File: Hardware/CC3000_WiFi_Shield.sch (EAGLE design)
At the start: 32 parts, among them J1 U.FL, U1 V_REG_317SMD, U2 ARDUINO_SHIELDLABEL, U3 74HC4050, U4 USD-SOCKETNEW, U5 CC3000

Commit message: Prototype board ready for review
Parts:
- C8: value 10pF -> DNP; COEFF C0G -> (none); PLACE DNP -> (none); TOL 5% -> (none)
- D1: value (none) -> GREEN; COLOR GREEN -> (none)
- JP1: value (none) -> Debug
- SJ1: value (none) -> Mode
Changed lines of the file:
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@@
 <setting verticaltext="up"/>
 </settings>
-<grid distance="0.1" unitdist="inch" unit="inch" style="lines" multiple="1" display="yes" altdistance="0.01" altunitdist="inch" altunit="inch"/>
+<grid distance="0.1" unitdist="inch" unit="inch" style="lines" multiple="1" display="no" altdistance="0.01" altunitdist="inch" altunit="inch"/>
 <layers>
 <layer number="1" name="Top" color="4" fill="1" visible="no" active="no"/>
@@
 <part name="SUPPLY5" library="SparkFun-Aesthetics" deviceset="3.3V" device=""/>
 <part name="GND9" library="SparkFun-Aesthetics" deviceset="GND" device=""/>
-<part name="SJ1" library="SparkFun-Passives" deviceset="SOLDERJUMPER_2WAY" device="PASTE1&amp;2"/>
+<part name="SJ1" library="SparkFun-Passives" deviceset="SOLDERJUMPER_2WAY" device="PASTE1&amp;2" value="Mode"/>
 <part name="GND10" library="SparkFun-Aesthetics" deviceset="GND" device=""/>
 <part name="GND11" library="SparkFun-Aesthetics" deviceset="GND" device=""/>
@@
 <part name="GND16" library="SparkFun-Aesthetics" deviceset="GND" device=""/>
 <part name="GND17" library="SparkFun-Aesthetics" deviceset="GND" device=""/>
-<part name="JP1" library="SparkFun-Connectors" deviceset="M03" device="PTH"/>
+<part name="JP1" library="SparkFun-Connectors" deviceset="M03" device="PTH" value="Debug"/>
 <part name="GND18" library="SparkFun-Aesthetics" deviceset="GND" device=""/>
-<part name="C8" library="SparkFun-Capacitors" deviceset="CAP" device="0603-CAP" value="10pF">
-<attribute name="COEFF" value="C0G"/>
-<attribute name="PLACE" value="DNP"/>
-<attribute name="TOL" value="5%"/>
-</part>
+<part name="C8" library="SparkFun-Capacitors" deviceset="CAP" device="0603-CAP" value="DNP"/>
 <part name="C7" library="SparkFun-Capacitors" deviceset="CAP" device="0603-CAP" value="2.2pF">
 <attribute name="COEFF" value="C0G"/>
@@
 <part name="R3" library="SparkFun-Resistors" deviceset="RESISTOR" device="0603-RES" value="390"/>
 <part name="GND19" library="SparkFun-Aesthetics" deviceset="GND" device=""/>
-<part name="D1" library="SparkFun-LED" deviceset="LED-GREEN" device="0603">
-<attribute name="COLOR" value="GREEN"/>
-</part>
+<part name="D1" library="SparkFun-LED" deviceset="LED-GREEN" device="0603" value="GREEN"/>
 <part name="R4" library="SparkFun-Resistors" deviceset="RESISTOR" device="0603-RES" value="10k"/>
 <part name="R5" library="SparkFun-Resistors" deviceset="RESISTOR" device="0603-RES" value="10k"/>
@@
 <instance part="GND16" gate="1" x="127" y="144.78"/>
 <instance part="GND17" gate="1" x="149.86" y="144.78"/>
-<instance part="JP1" gate="G$1" x="38.1" y="121.92" rot="MR180"/>
+<instance part="JP1" gate="G$1" x="38.1" y="121.92" smashed="yes" rot="MR180">
+<attribute name="VALUE" x="25.4" y="127" size="1.778" layer="96" rot="MR180"/>
+<attribute name="NAME" x="35.56" y="116.078" size="1.778" layer="95" rot="MR180"/>
+</instance>
 <instance part="GND18" gate="1" x="50.8" y="114.3"/>
 <instance part="C8" gate="G$1" x="182.88" y="167.64" smashed="yes" rot="R90">
-<attribute name="COEFF" x="182.88" y="160.02" size="1.778" layer="96"/>
-<attribute name="TOL" x="182.88" y="162.56" size="1.778" layer="96"/>
 <attribute name="NAME" x="177.8" y="170.307" size="1.778" layer="95"/>
 <attribute name="VALUE" x="182.88" y="165.227" size="1.778" layer="96"/>
-<attribute name="PLACE" x="182.88" y="170.18" size="1.778" layer="96"/>
 </instance>
 <instance part="C7" gate="G$1" x="139.7" y="167.64" smashed="yes" rot="R90">
@@
 <instance part="GND19" gate="1" x="83.82" y="142.24"/>
 <instance part="D1" gate="G$1" x="83.82" y="157.48" smashed="yes">
-<attribute name="COLOR" x="86.36" y="154.94" size="1.778" layer="96"/>
 <attribute name="NAME" x="86.36" y="157.48" size="1.778" layer="95"/>
-<attribute name="VALUE" x="89.535" y="152.908" size="1.778" layer="96" rot="R90"/>
+<attribute name="VALUE" x="86.106" y="154.305" size="1.778" layer="96"/>
 </instance>
 <instance part="R4" gate="G$1" x="53.34" y="33.02" smashed="yes" rot="R90">
@@
 <wire x1="60.96" y1="175.26" x2="60.96" y2="172.72" width="0.1524" layer="91"/>
 <junction x="50.8" y="175.26"/>
-<pinref part="C4" gate="G$1" pin="1"/>
+<junction x="60.96" y="175.26"/>
+<pinref part="R3" gate="G$1" pin="2"/>
 <wire x1="60.96" y1="175.26" x2="71.12" y2="175.26" width="0.1524" layer="91"/>
-<wire x1="71.12" y1="175.26" x2="71.12" y2="172.72" width="0.1524" layer="91"/>
-<junction x="60.96" y="175.26"/>
-<junction x="71.12" y="175.26"/>
-<wire x1="71.12" y1="172.72" x2="71.12" y2="170.18" width="0.1524" layer="91"/>
-<pinref part="R3" gate="G$1" pin="2"/>
 <wire x1="71.12" y1="175.26" x2="83.82" y2="175.26" width="0.1524" layer="91"/>
 <wire x1="83.82" y1="175.26" x2="83.82" y2="172.72" width="0.1524" layer="91"/>
@@
 <wire x1="83.82" y1="177.8" x2="83.82" y2="175.26" width="0.1524" layer="91"/>
 <junction x="83.82" y="175.26"/>
+<pinref part="C4" gate="G$1" pin="1"/>
+<wire x1="71.12" y1="172.72" x2="71.12" y2="175.26" width="0.1524" layer="91"/>
+<junction x="71.12" y="175.26"/>
 </segment>
 <segment>
@@
 </sheet>
 </sheets>
+<errors>
+</errors>
 </schematic>
 </drawing>

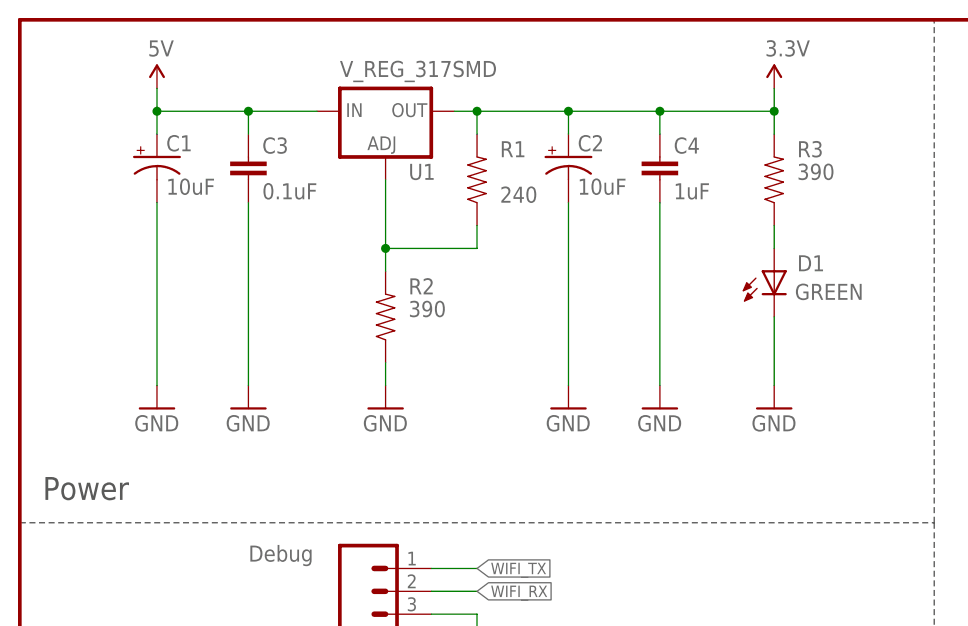
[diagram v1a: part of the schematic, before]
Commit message: Fixed floating 3.3V paddle on LM317. Made stitching vias near RF section 10 mils.
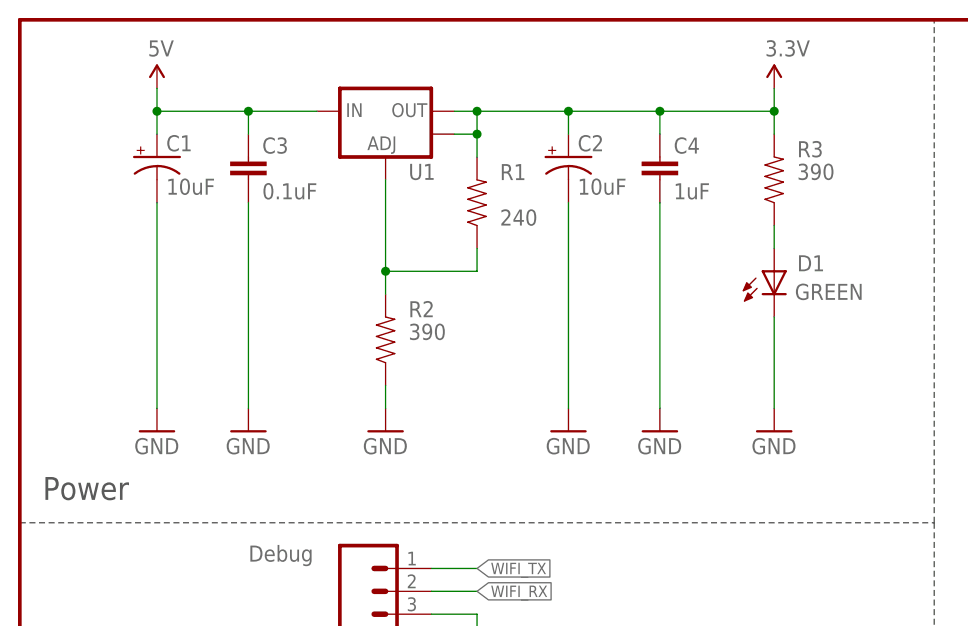
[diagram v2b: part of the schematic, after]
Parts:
- U1: value V_REG_317SMD -> (none); device SparkFun-PowerIC:V_REG_317SMD -> SparkFun-PowerIC:V_REG_LM1117SOT223
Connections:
- net 3.3V: now also U1.OUT@1
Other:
- moved on the sheet: R1, R2
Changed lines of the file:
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@@
 <part name="R1" library="SparkFun-Resistors" deviceset="RESISTOR" device="0603" value="240"/>
 <part name="R2" library="SparkFun-Resistors" deviceset="RESISTOR" device="0603" value="390"/>
-<part name="U1" library="SparkFun-PowerIC" deviceset="V_REG_317" device="SMD"/>
+<part name="U1" library="SparkFun-PowerIC" deviceset="V_REG_LM1117" device="SOT223"/>
 <part name="GND1" library="SparkFun-Aesthetics" deviceset="GND" device=""/>
 <part name="GND2" library="SparkFun-Aesthetics" deviceset="GND" device=""/>
@@
 <instance part="C3" gate="G$1" x="25.4" y="167.64"/>
 <instance part="C4" gate="G$1" x="71.12" y="167.64"/>
-<instance part="R1" gate="G$1" x="50.8" y="167.64" smashed="yes" rot="R90">
-<attribute name="NAME" x="53.34" y="170.1546" size="1.778" layer="95"/>
-<attribute name="VALUE" x="53.34" y="165.1" size="1.778" layer="96"/>
-</instance>
-<instance part="R2" gate="G$1" x="40.64" y="152.4" smashed="yes" rot="R90">
-<attribute name="NAME" x="43.18" y="154.9146" size="1.778" layer="95"/>
-<attribute name="VALUE" x="43.18" y="152.4" size="1.778" layer="96"/>
+<instance part="R1" gate="G$1" x="50.8" y="165.1" smashed="yes" rot="R90">
+<attribute name="NAME" x="53.34" y="167.6146" size="1.778" layer="95"/>
+<attribute name="VALUE" x="53.34" y="162.56" size="1.778" layer="96"/>
+</instance>
+<instance part="R2" gate="G$1" x="40.64" y="149.86" smashed="yes" rot="R90">
+<attribute name="NAME" x="43.18" y="152.3746" size="1.778" layer="95"/>
+<attribute name="VALUE" x="43.18" y="149.86" size="1.778" layer="96"/>
 </instance>
 <instance part="U1" gate="G$1" x="40.64" y="175.26" smashed="yes">
@@
 <attribute name="VALUE" x="35.56" y="179.07" size="1.778" layer="96"/>
 </instance>
-<instance part="GND1" gate="1" x="40.64" y="142.24"/>
-<instance part="GND2" gate="1" x="25.4" y="142.24"/>
-<instance part="GND3" gate="1" x="15.24" y="142.24"/>
-<instance part="GND4" gate="1" x="60.96" y="142.24"/>
-<instance part="GND5" gate="1" x="71.12" y="142.24"/>
+<instance part="GND1" gate="1" x="40.64" y="139.7"/>
+<instance part="GND2" gate="1" x="25.4" y="139.7"/>
+<instance part="GND3" gate="1" x="15.24" y="139.7"/>
+<instance part="GND4" gate="1" x="60.96" y="139.7"/>
+<instance part="GND5" gate="1" x="71.12" y="139.7"/>
 <instance part="U3" gate="G$1" x="22.86" y="20.32"/>
 <instance part="GND6" gate="1" x="43.18" y="30.48"/>
@@
 <attribute name="VALUE" x="86.36" y="167.64" size="1.778" layer="96"/>
 </instance>
-<instance part="GND19" gate="1" x="83.82" y="142.24"/>
+<instance part="GND19" gate="1" x="83.82" y="139.7"/>
 <instance part="D1" gate="G$1" x="83.82" y="157.48" smashed="yes">
 <attribute name="NAME" x="86.36" y="157.48" size="1.778" layer="95"/>
@@
 <pinref part="U1" gate="G$1" pin="ADJ"/>
 <pinref part="R2" gate="G$1" pin="2"/>
-<wire x1="40.64" y1="167.64" x2="40.64" y2="160.02" width="0.1524" layer="91"/>
+<wire x1="40.64" y1="167.64" x2="40.64" y2="157.48" width="0.1524" layer="91"/>
 <pinref part="R1" gate="G$1" pin="1"/>
-<wire x1="40.64" y1="160.02" x2="40.64" y2="157.48" width="0.1524" layer="91"/>
-<wire x1="50.8" y1="162.56" x2="50.8" y2="160.02" width="0.1524" layer="91"/>
-<wire x1="50.8" y1="160.02" x2="40.64" y2="160.02" width="0.1524" layer="91"/>
-<junction x="40.64" y="160.02"/>
+<wire x1="40.64" y1="157.48" x2="40.64" y2="154.94" width="0.1524" layer="91"/>
+<wire x1="50.8" y1="160.02" x2="50.8" y2="157.48" width="0.1524" layer="91"/>
+<wire x1="50.8" y1="157.48" x2="40.64" y2="157.48" width="0.1524" layer="91"/>
+<junction x="40.64" y="157.48"/>
 </segment>
 </net>
@@
 <wire x1="50.8" y1="175.26" x2="50.8" y2="172.72" width="0.1524" layer="91"/>
 <pinref part="C2" gate="G$1" pin="+"/>
+<wire x1="50.8" y1="172.72" x2="50.8" y2="170.18" width="0.1524" layer="91"/>
 <wire x1="50.8" y1="175.26" x2="60.96" y2="175.26" width="0.1524" layer="91"/>
 <wire x1="60.96" y1="175.26" x2="60.96" y2="172.72" width="0.1524" layer="91"/>
@@
 <wire x1="71.12" y1="172.72" x2="71.12" y2="175.26" width="0.1524" layer="91"/>
 <junction x="71.12" y="175.26"/>
+<pinref part="U1" gate="G$1" pin="OUT@1"/>
+<wire x1="48.26" y1="172.72" x2="50.8" y2="172.72" width="0.1524" layer="91"/>
+<junction x="50.8" y="172.72"/>
 </segment>
 <segment>
@@
 <pinref part="C1" gate="G$1" pin="-"/>
 <pinref part="GND3" gate="1" pin="GND"/>
-<wire x1="15.24" y1="165.1" x2="15.24" y2="144.78" width="0.1524" layer="91"/>
+<wire x1="15.24" y1="165.1" x2="15.24" y2="142.24" width="0.1524" layer="91"/>
 </segment>
 <segment>
 <pinref part="C3" gate="G$1" pin="2"/>
 <pinref part="GND2" gate="1" pin="GND"/>
-<wire x1="25.4" y1="165.1" x2="25.4" y2="144.78" width="0.1524" layer="91"/>
+<wire x1="25.4" y1="165.1" x2="25.4" y2="142.24" width="0.1524" layer="91"/>
 </segment>
 <segment>
 <pinref part="R2" gate="G$1" pin="1"/>
 <pinref part="GND1" gate="1" pin="GND"/>
-<wire x1="40.64" y1="147.32" x2="40.64" y2="144.78" width="0.1524" layer="91"/>
+<wire x1="40.64" y1="144.78" x2="40.64" y2="142.24" width="0.1524" layer="91"/>
 </segment>
 <segment>
 <pinref part="C2" gate="G$1" pin="-"/>
 <pinref part="GND4" gate="1" pin="GND"/>
-<wire x1="60.96" y1="165.1" x2="60.96" y2="144.78" width="0.1524" layer="91"/>
+<wire x1="60.96" y1="165.1" x2="60.96" y2="142.24" width="0.1524" layer="91"/>
 </segment>
 <segment>
 <pinref part="C4" gate="G$1" pin="2"/>
 <pinref part="GND5" gate="1" pin="GND"/>
-<wire x1="71.12" y1="165.1" x2="71.12" y2="144.78" width="0.1524" layer="91"/>
+<wire x1="71.12" y1="165.1" x2="71.12" y2="142.24" width="0.1524" layer="91"/>
 </segment>
 <segment>
@@
 <pinref part="D1" gate="G$1" pin="C"/>
 <pinref part="GND19" gate="1" pin="GND"/>
-<wire x1="83.82" y1="152.4" x2="83.82" y2="144.78" width="0.1524" layer="91"/>
+<wire x1="83.82" y1="152.4" x2="83.82" y2="142.24" width="0.1524" layer="91"/>
 </segment>
 </net>
